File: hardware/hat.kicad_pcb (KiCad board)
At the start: 4 copper layers, 65 x 56.6 mm, 144 parts, among them J101 Raspberry_Pi_2_3, J102 Boot, J201 USB Power In, K201 CONN_3, P101 Debug, P201 Black, P301 CON-SENSOR2, P302 CON-SENSOR2, P303 CON-SENSOR2, P304 CON-SENSOR2, P305 CON-SENSOR2, P306 CON-SENSOR2, P307 CON-SENSOR2, P308 CON-SENSOR2, Q101 2N7002P, Q102 2N7002P, Q103 NTR2101P, Q104 NTR2101P, U101 XMC1404, U102 LD1117, U201 MAX17260_LS, U202 BQ2407X, U203 AOZ1212, U204 MIC2253, U205 AP7333-33SAG-7, U301 74AHC244, U302 74AHC244, U303 74AHC244, U304 74AHC244, X101 16MHz, X102 32.768kHz

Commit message: routing and thermal optimzations
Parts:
- moved RP102 1.00 mm to (188.0, 35.9)
- moved RP103 1.00 mm to (212.0, 35.9)
- moved RP104 1.00 mm to (200.0, 35.9)
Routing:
- net GND: track 449.2 -> 479.7 mm, vias 379 -> 393
- net USB-IN-VOLTAGE: track 74.2 -> 64.5 mm
- net Net-(J101-Pad31): track 3.00 -> 5.52 mm
- net RASP-PWR: track 22.0 -> 19.7 mm
- net B-CS0: track 20.6 -> 18.8 mm
- net Net-(J101-Pad21): track 2.92 -> 3.93 mm
- net Net-(J101-Pad29): track 3.76 -> 4.76 mm
- net Net-(J101-Pad26): track 12.9 -> 13.9 mm
- net Net-(J101-Pad23): track 4.26 -> 5.26 mm
- net Net-(J101-Pad22): track 12.1 -> 13.1 mm
- net Net-(J101-Pad19): track 5.06 -> 6.06 mm
- net B-MOSI: track 89.8 -> 88.8 mm
- net B-MISO: track 88.7 -> 87.7 mm
- net B-CS5: track 15.7 -> 14.7 mm
- net B-CLK: track 85.9 -> 84.9 mm
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- added copper zone on B.Cu, net B-3V3

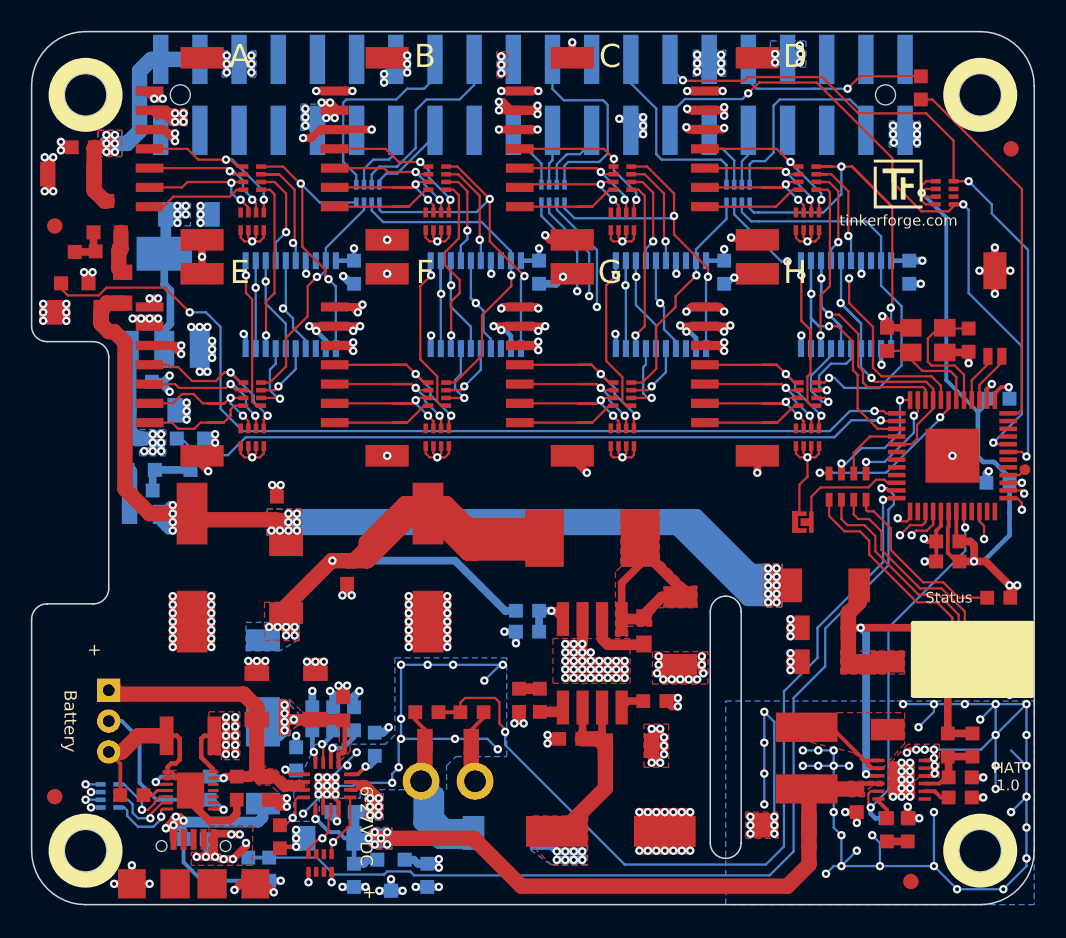
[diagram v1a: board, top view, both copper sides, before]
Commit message: fix battery connector
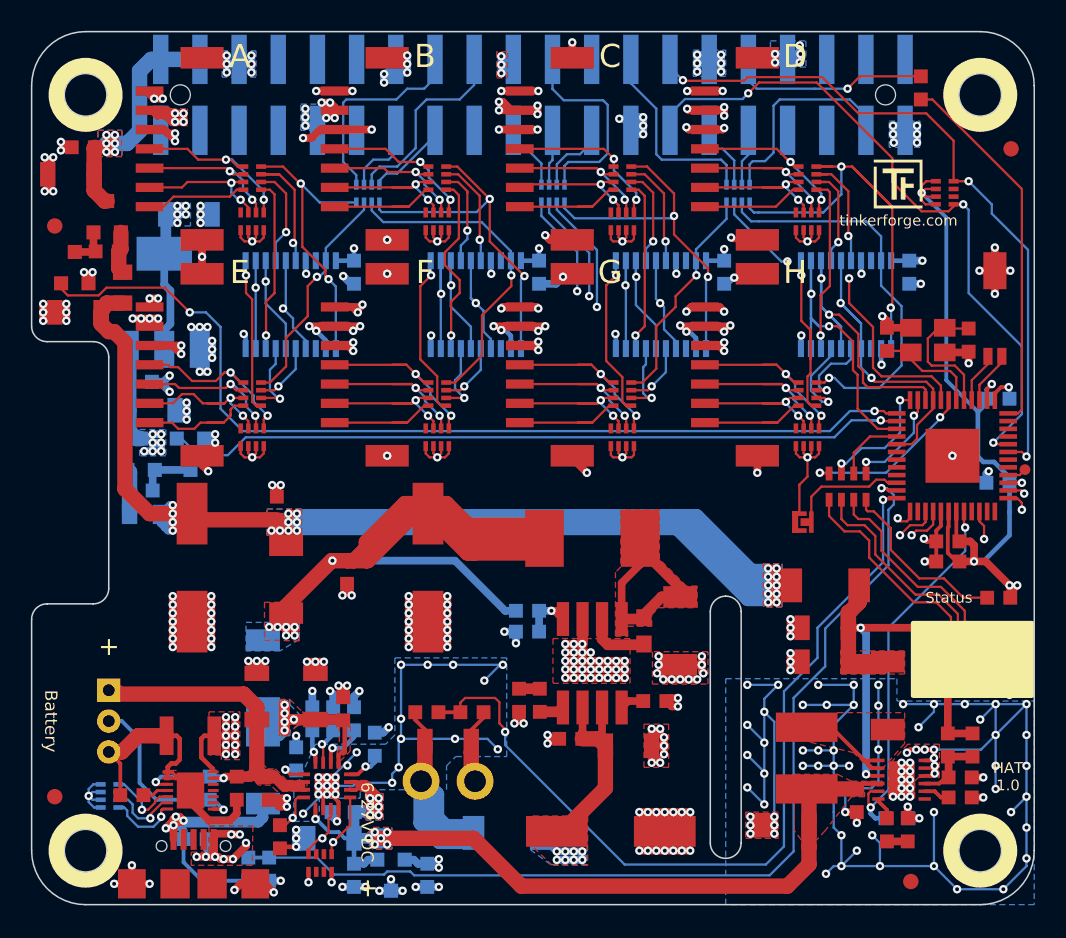
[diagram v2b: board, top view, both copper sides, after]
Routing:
- net GND: track 479.7 -> 507.5 mm, vias 393 -> 405
- net 3V3: track 145.6 -> 127.2 mm, vias 15 -> 12
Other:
- board text added: "DNP? 16MHz"
- board text removed: "-"
- board text removed: "OVP, Switch?"
- board text removed: "Stecker falsch herum?"

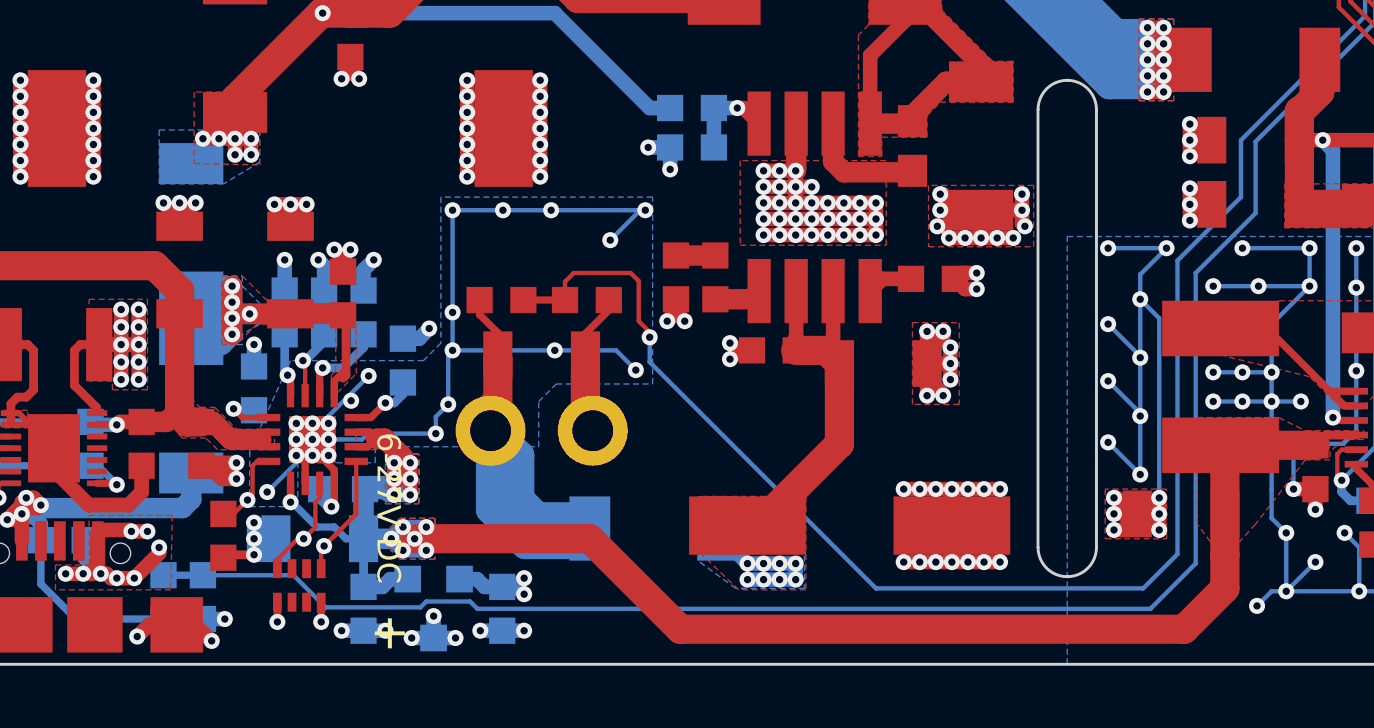
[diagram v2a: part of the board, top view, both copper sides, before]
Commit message: add slide switch for sysoff
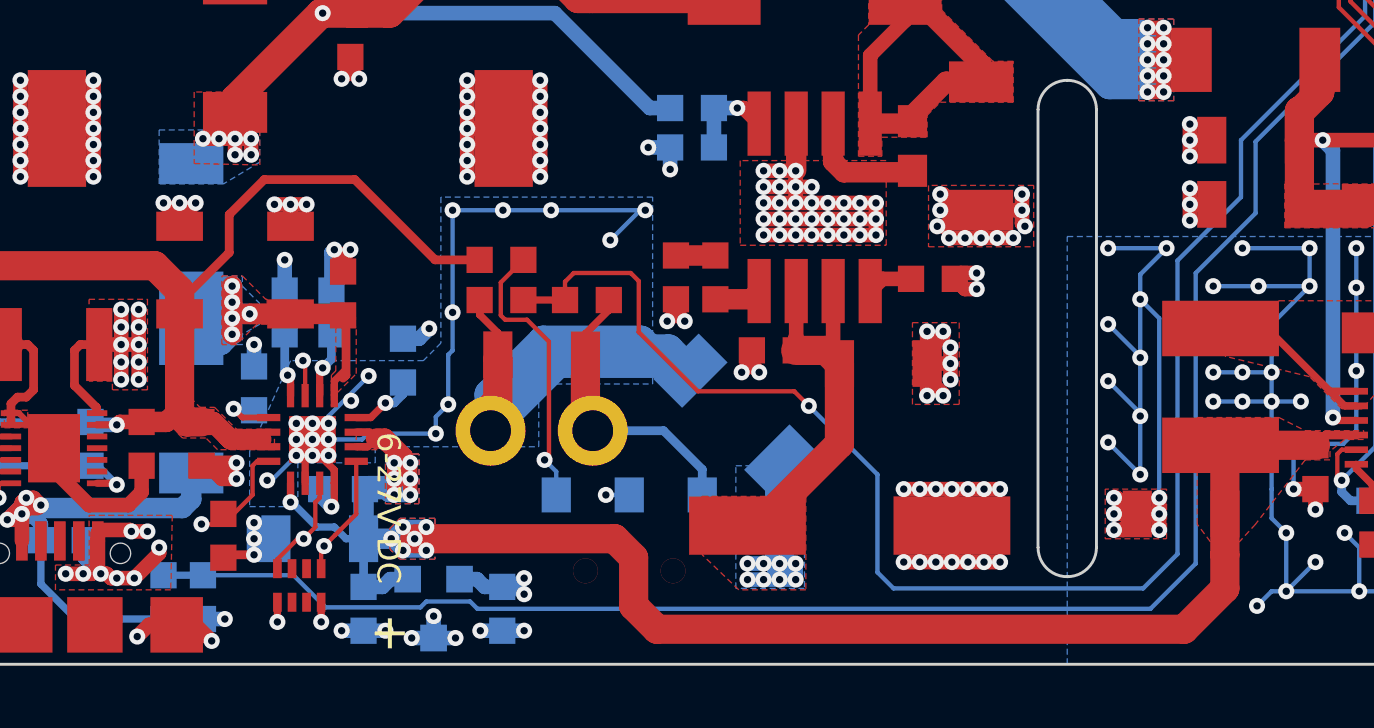
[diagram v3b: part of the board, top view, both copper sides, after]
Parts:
- added S201: SWITCH_SPDT, SW-SLIDE-SMD, B.Cu at (196.2, 78.8)
- R219: moved to F.Cu
- moved R219 6.34 mm to (191.8, 68.2), turned to 180 degrees
- moved D203 4.76 mm to (199.8, 73.5), turned to 135 degrees
- moved R209 1.10 mm to (186.0, 70.0)
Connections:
- R219 pad 2: GND -> BATTERY-OUT
- U202 pad 15: Net-(R219-Pad1) -> SYSOFF
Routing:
- net SYSOFF: track 0.00 -> 21.9 mm, vias 0 -> 2
- net BATTERY-OUT: track 29.8 -> 44.1 mm
- net Net-(R219-Pad1): track 2.48 -> 9.72 mm
- net Net-(D203-Pad1): track 20.3 -> 24.7 mm
- net GND: track 507.5 -> 503.1 mm, vias 405 -> 400
- net CHG-EN: track 65.3 -> 69.1 mm
- net STEP-IN: track 18.8 -> 20.8 mm
- net DC-IN-VOLTAGE: track 55.6 -> 57.2 mm
- net BOOST-IN: track 61.9 -> 62.9 mm
- net Net-(R209-Pad2): track 3.13 -> 2.27 mm
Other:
- board text added: "Add Switch Text"

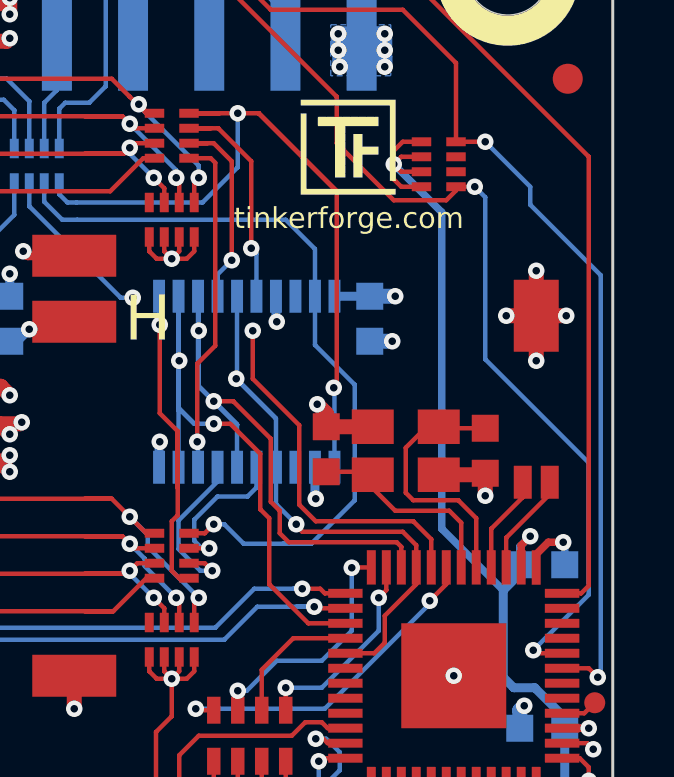
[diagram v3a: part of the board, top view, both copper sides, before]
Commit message: remove 16mhz crystal, add capacitors for 32kHz Crystal
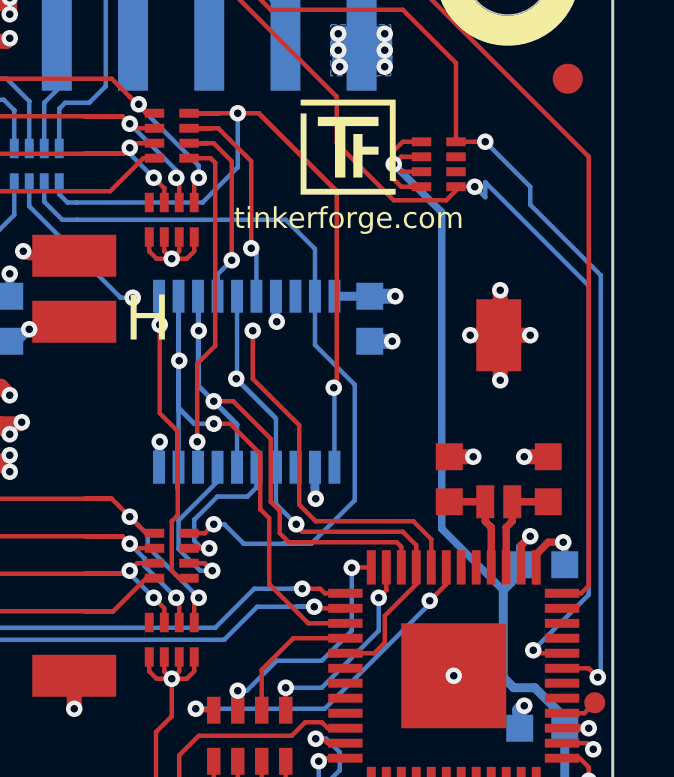
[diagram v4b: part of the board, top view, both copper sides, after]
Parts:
- removed X102: 32.768kHz, kicad-libraries:AB26TRQ
- C105, C106: value 10pF -> TBD
- X101: value 16MHz -> 32.768kHz; footprint kicad-libraries:CRYSTAL_3225 -> kicad-libraries:AB26TRQ
- moved X101 4.94 mm to (227.4, 41.5)
- moved C105 4.22 mm to (225.8, 46.4)
- moved C106 2.30 mm to (229.1, 46.4), turned to 270 degrees
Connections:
- U101 pad 39: Net-(U101-Pad39) -> Net-(C106-Pad2)
- U101 pad 40: Net-(U101-Pad40) -> Net-(C105-Pad2)
- U101 pad 41: Net-(C106-Pad2) -> (no net)
- U101 pad 42: Net-(C105-Pad2) -> (no net)
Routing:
- net Net-(C106-Pad2): track 8.80 -> 3.47 mm
- net Net-(C105-Pad2): track 6.96 -> 3.47 mm
- net Net-(U101-Pad39): track 3.44 -> 0.00 mm
- net Net-(U101-Pad40): track 3.27 -> 0.00 mm
- net GND: track 503.1 -> 499.9 mm
- net RASP-SD: track 44.5 -> 45.5 mm
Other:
- board text removed: "DNP? 16MHz"

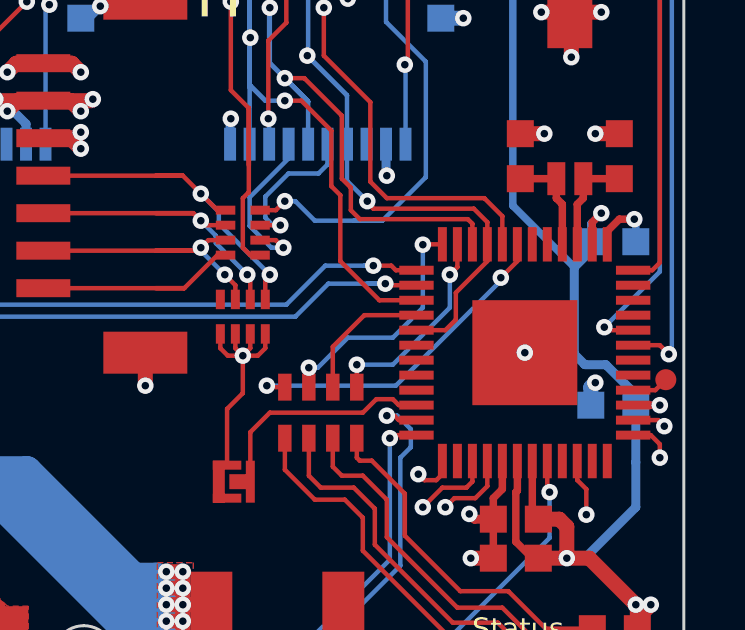
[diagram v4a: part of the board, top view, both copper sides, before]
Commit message: change additional bricklet clock pin to P0.6
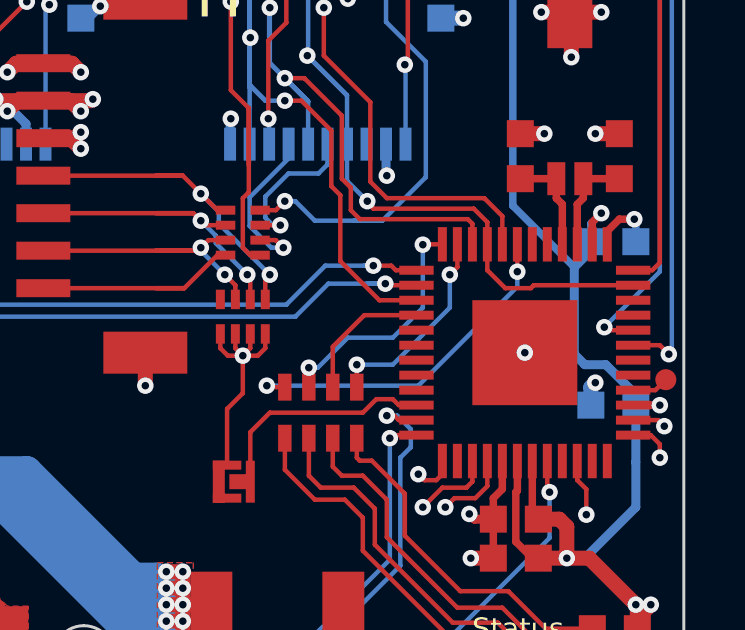
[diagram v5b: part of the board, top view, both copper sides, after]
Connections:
- U101 pad 35: (no net) -> B-CLK
- U101 pad 5: B-CLK -> (no net)
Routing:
- net B-CLK: track 84.9 -> 86.5 mm
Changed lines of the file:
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@@
     (pad 4 smd rect (at -1.24968 3.61188 90) (size 0.29972 1.14808) (layers F.Cu F.Paste F.Mask)
       (net 142 "Net-(RP105-Pad3)"))
-    (pad 5 smd rect (at -0.7493 3.61188 90) (size 0.29972 1.14808) (layers F.Cu F.Paste F.Mask)
-      (net 105 B-CLK))
+    (pad 5 smd rect (at -0.7493 3.61188 90) (size 0.29972 1.14808) (layers F.Cu F.Paste F.Mask))
     (pad 6 smd rect (at -0.24892 3.61188 90) (size 0.29972 1.14808) (layers F.Cu F.Paste F.Mask))
     (pad 7 smd rect (at 0.24892 3.61188 90) (size 0.29972 1.14808) (layers F.Cu F.Paste F.Mask))
@@
     (pad 33 smd rect (at -1.24968 -3.61188 270) (size 0.29972 1.14808) (layers F.Cu F.Paste F.Mask))
     (pad 34 smd rect (at -1.74752 -3.61188 270) (size 0.29972 1.14808) (layers F.Cu F.Paste F.Mask))
-    (pad 35 smd rect (at -2.2479 -3.61188 270) (size 0.29972 1.14808) (layers F.Cu F.Paste F.Mask))
+    (pad 35 smd rect (at -2.2479 -3.61188 270) (size 0.29972 1.14808) (layers F.Cu F.Paste F.Mask)
+      (net 105 B-CLK))
     (pad 36 smd rect (at -2.74828 -3.61188 270) (size 0.29972 1.14808) (layers F.Cu F.Paste F.Mask)
       (net 122 RASP-GP))
@@
   (segment (start 206.67742 42.72742) (end 206.95 43) (width 0.15) (layer B.Cu) (net 105))
   (via (at 206.95 43) (size 0.55) (drill 0.25) (layers F.Cu B.Cu) (net 105))
-  (segment (start 222.28812 52.1507) (end 223.2493 52.1507) (width 0.15) (layer F.Cu) (net 105))
-  (segment (start 224.65032 49.84968) (end 224.65032 49.28812) (width 0.15) (layer F.Cu) (net 105))
-  (segment (start 223.6 50.9) (end 224.65032 49.84968) (width 0.15) (layer F.Cu) (net 105))
-  (segment (start 223.6 51.8) (end 223.6 50.9) (width 0.15) (layer F.Cu) (net 105))
-  (segment (start 223.2493 52.1507) (end 223.6 51.8) (width 0.15) (layer F.Cu) (net 105))
   (segment (start 220.7 47.95) (end 220.7 47.9) (width 0.15) (layer F.Cu) (net 105))
   (segment (start 224.65032 48.55032) (end 224.2 48.1) (width 0.15) (layer F.Cu) (net 105))
@@
   (segment (start 202.85 39.55) (end 202.85 43.25) (width 0.15) (layer B.Cu) (net 105))
   (segment (start 200.24892 36.94892) (end 202.85 39.55) (width 0.15) (layer B.Cu) (net 105))
+  (segment (start 224.65032 49.28812) (end 224.65032 50.15032) (width 0.15) (layer F.Cu) (net 105) (status 400000))
+  (segment (start 226.1979 50.6521) (end 229.51188 50.6521) (width 0.15) (layer F.Cu) (net 105) (status 800000))
+  (segment (start 226.1 50.75) (end 226.1979 50.6521) (width 0.15) (layer F.Cu) (net 105))
+  (segment (start 225.25 50.75) (end 226.1 50.75) (width 0.15) (layer F.Cu) (net 105))
+  (segment (start 224.65032 50.15032) (end 225.25 50.75) (width 0.15) (layer F.Cu) (net 105))
   (segment (start 217.37694 40.25012) (end 217.4 40.27318) (width 0.15) (layer B.Cu) (net 106))
   (segment (start 217.4 40.27318) (end 217.4 41.4) (width 0.15) (layer B.Cu) (net 106))
@@
   (segment (start 223.4 51.4) (end 223.4 50.3) (width 0.15) (layer B.Cu) (net 139))
   (segment (start 221.5 53.3) (end 223.4 51.4) (width 0.15) (layer B.Cu) (net 139))
-  (segment (start 225.1 50.4) (end 225.1 50.5) (width 0.15) (layer B.Cu) (net 140))
-  (via (at 225.1 50.4) (size 0.55) (drill 0.25) (layers F.Cu B.Cu) (net 140))
-  (segment (start 225.65108 49.84892) (end 225.1 50.4) (width 0.15) (layer F.Cu) (net 140))
   (segment (start 217.3491 54.0491) (end 217.3 54) (width 0.15) (layer F.Cu) (net 140))
-  (via (at 217.3 54) (size 0.55) (drill 0.25) (layers F.Cu B.Cu) (net 140))
   (segment (start 217.3491 54.0491) (end 217.90112 54.0491) (width 0.15) (layer F.Cu) (net 140))
-  (segment (start 221.6 54) (end 217.3 54) (width 0.15) (layer B.Cu) (net 140))
-  (segment (start 225.1 50.5) (end 221.6 54) (width 0.15) (layer B.Cu) (net 140))
-  (segment (start 225.65108 49.28812) (end 225.65108 49.84892) (width 0.15) (layer F.Cu) (net 140))
+  (via (at 217.3 54) (size 0.55) (drill 0.25) (layers F.Cu B.Cu) (net 140))
+  (segment (start 225.65108 49.28812) (end 225.65 49.2892) (width 0.15) (layer F.Cu) (net 140) (status C00000))
+  (segment (start 222.35 54) (end 217.3 54) (width 0.15) (layer B.Cu) (net 140))
+  (segment (start 225.65 50.7) (end 222.35 54) (width 0.15) (layer B.Cu) (net 140))
+  (segment (start 225.65 50.2) (end 225.65 50.7) (width 0.15) (layer B.Cu) (net 140))
+  (via (at 225.65 50.2) (size 0.55) (drill 0.25) (layers F.Cu B.Cu) (net 140))
+  (segment (start 225.65 49.2892) (end 225.65 50.2) (width 0.15) (layer F.Cu) (net 140) (status 400000))
   (segment (start 218.7 53.4) (end 219 53.4) (width 0.15) (layer B.Cu) (net 141))
   (segment (start 222.51188 49.28812) (end 222.5 49.3) (width 0.15) (layer F.Cu) (net 141))
